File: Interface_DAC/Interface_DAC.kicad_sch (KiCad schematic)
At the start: 57 parts, among them SW1 SW_Push, SW2 SW_DIP_x02, U1 MIMXRT1011DAE5A, U2 W25Q32JVUU, U3 UM803RS, Y1 KC2520Z, Y2 KC2520Z, Y3 24M

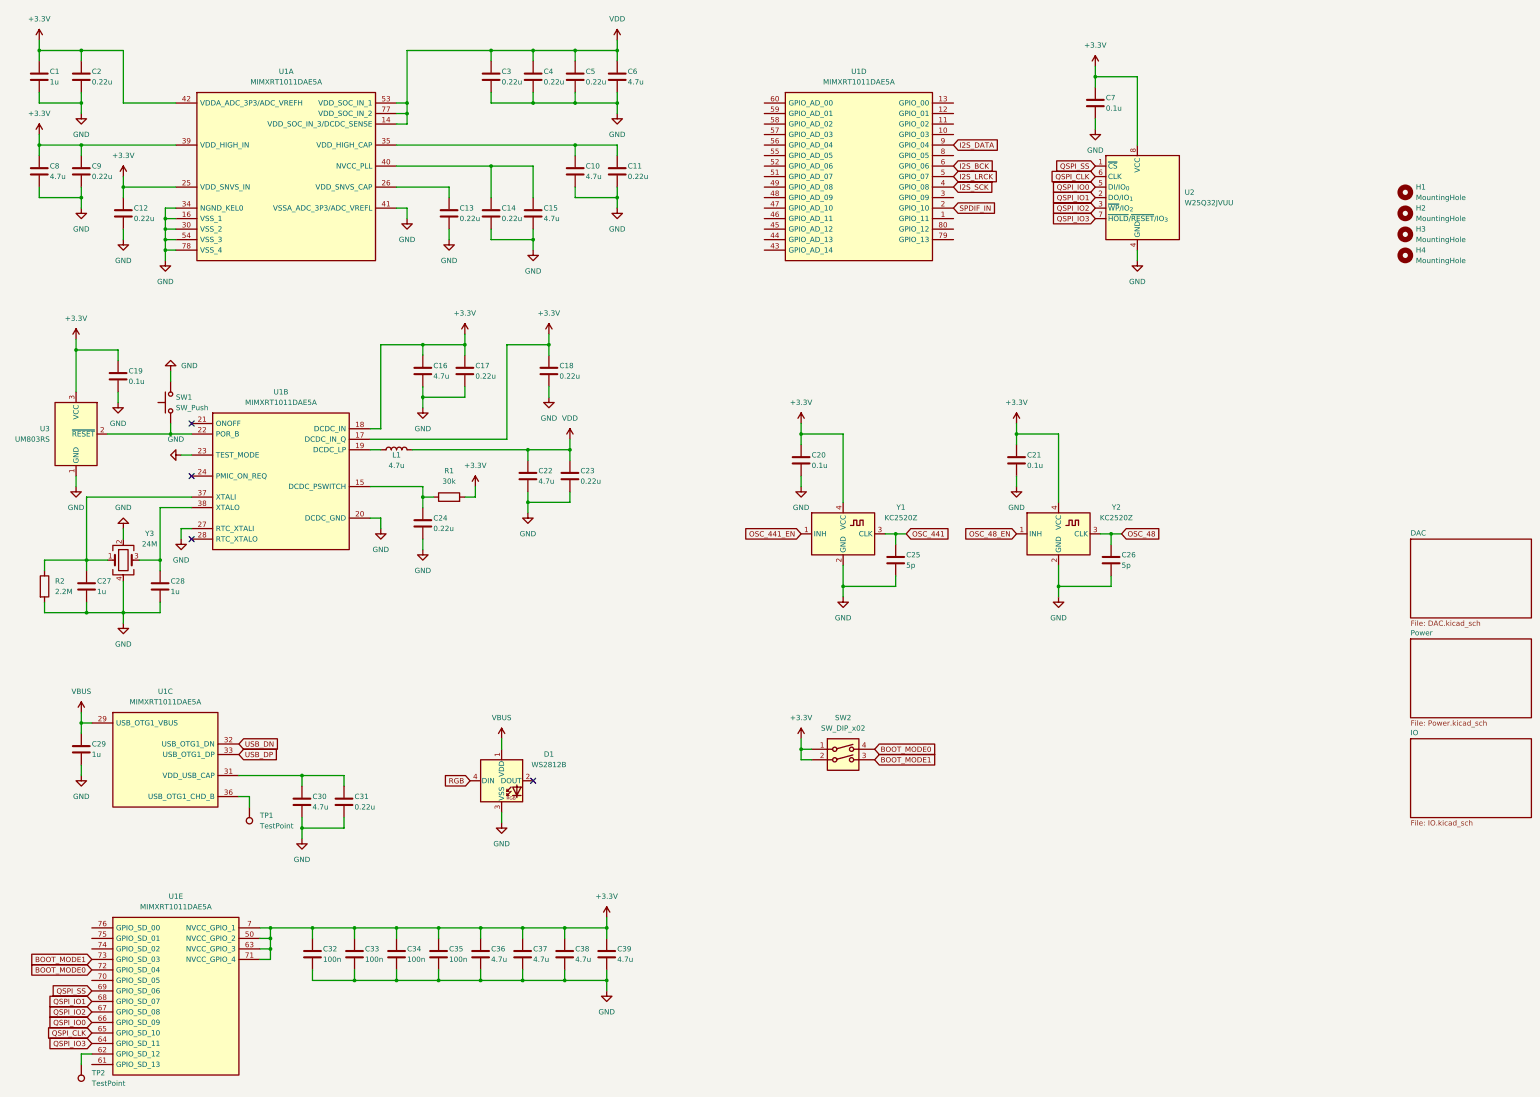
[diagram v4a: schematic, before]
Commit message: Microcontroller Swap
Changed the microcontroller from NXP MIMXRT1011DAE5A to ST STM32F446RET6
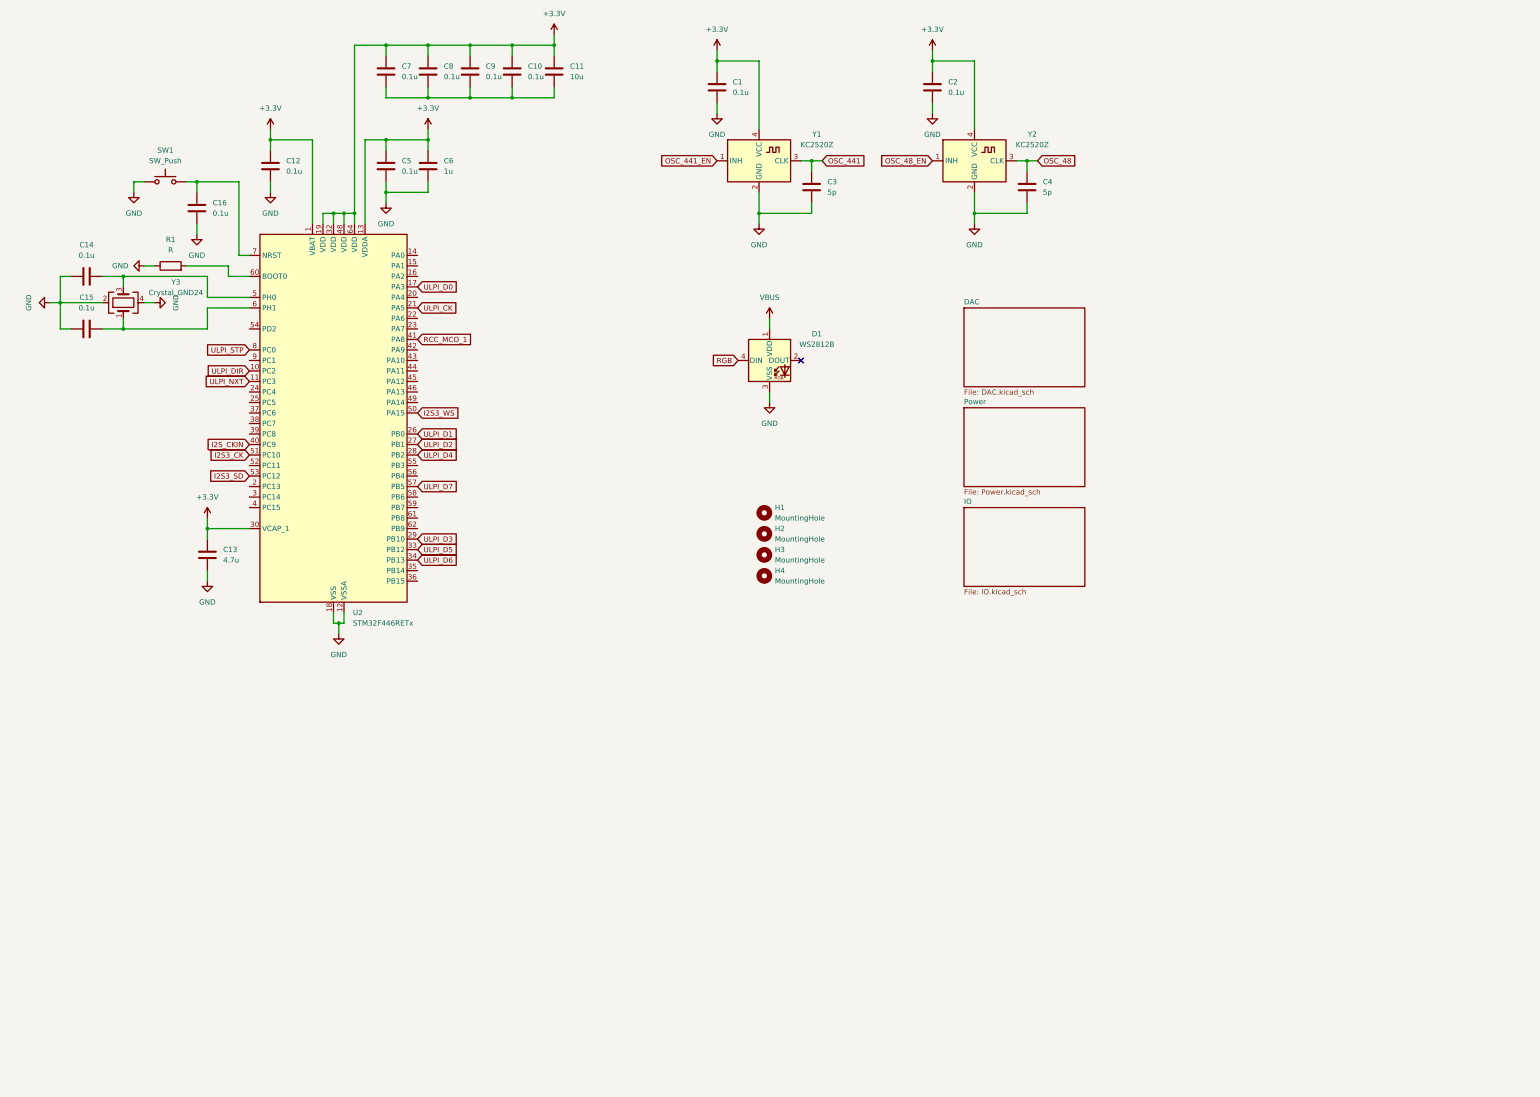
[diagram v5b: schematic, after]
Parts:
- removed C17, C18, C23, C24, C31: 0.22u, Capacitor_SMD:C_0402_1005Metric, symbol Device:C
- removed C19, C20, C21: 0.1u, Capacitor_SMD:C_0402_1005Metric, symbol Device:C
- removed C22, C30, C36, C37, C38, C39: 4.7u, Capacitor_SMD:C_0402_1005Metric, symbol Device:C
- removed C25, C26: 5p, Capacitor_SMD:C_0402_1005Metric, symbol Device:C
- removed C27, C28, C29: 1u, Capacitor_SMD:C_0402_1005Metric, symbol Device:C
- removed C32, C33, C34, C35: 100n, Capacitor_SMD:C_0402_1005Metric, symbol Device:C
- removed L1: 4.7u, Inductor_SMD:L_Murata_DFE201610P, symbol Device:L
- removed R2: 2.2M, Resistor_SMD:R_0402_1005Metric, symbol Device:R
- removed SW2: SW_DIP_x02, Button_Switch_SMD:SW_DIP_SPSTx02_Slide_Copal_CHS-02B_W7.62mm_P1.27mm, symbol Switch:SW_DIP_x02
- removed TP1, TP2: TestPoint, TestPoint:TestPoint_Pad_D1.0mm, symbol Connector:TestPoint
- removed U1: MIMXRT1011DAE5A, Package_QFP:LQFP-80_12x12mm_P0.5mm, symbol utils:MIMXRT1011DAE5A
- removed U2: W25Q32JVUU, Package_SON:Winbond_USON-8-2EP_3x4mm_P0.8mm_EP0.2x0.8mm, symbol Memory_Flash:W25Q32JVSS
- removed U3: UM803RS, Package_TO_SOT_SMD:SOT-23, symbol utils:UM803RS
- added U2: STM32F446RETx, Package_QFP:LQFP-64_10x10mm_P0.5mm, symbol MCU_ST_STM32F4:STM32F446RETx
- C1: value 1u -> 0.1u; footprint Capacitor_SMD:C_0402_1005Metric -> (none)
- C10, C15, C16, C8: value 4.7u -> 0.1u; footprint Capacitor_SMD:C_0402_1005Metric -> (none)
- C11: value 0.22u -> 10u; footprint Capacitor_SMD:C_0402_1005Metric -> (none)
- C12, C14, C2, C5, C9: value 0.22u -> 0.1u; footprint Capacitor_SMD:C_0402_1005Metric -> (none)
- C13: value 0.22u -> 4.7u; footprint Capacitor_SMD:C_0402_1005Metric -> (none)
- C3, C4: value 0.22u -> 5p; footprint Capacitor_SMD:C_0402_1005Metric -> (none)
- C6: value 4.7u -> 1u; footprint Capacitor_SMD:C_0402_1005Metric -> (none)
- C7: footprint Capacitor_SMD:C_0402_1005Metric -> (none)
- R1: value 30k -> R; footprint Resistor_SMD:R_0402_1005Metric -> (none)
- SW1: footprint Connector_PinHeader_1.27mm:PinHeader_1x02_P1.27mm_Vertical -> (none)
- Y3: value 24M -> Crystal_GND24; footprint Oscillator:Oscillator_SMD_Kyocera_KC2520Z-4Pin_2.5x2.0mm -> (none)
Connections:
- net +3.3V: now also C10.1, C11.1, C13.1, C5.1, C6.1, U2.1 (VBAT), U2.13 (VDDA), U2.19 (VDD), U2.30 (VCAP_1), U2.32 (VDD), U2.48 (VDD), U2.64 (VDD); no longer C16.1, R1.2
- net GND: now also C14.1, C15.1, R1.1, SW1.1, U2.12 (VSSA), U2.18 (VSS), U2.31 (VSS), U2.47 (VSS), U2.63 (VSS); no longer C10.2, C11.2, C14.2, C15.2, C7.2, C8.2, C9.2, SW1.2
- net OSC_441: now also C3.1
- net OSC_48: now also C4.1
- net at Y3.1: now also C15.2, U2.6 (PH1)
- net at Y3.3: now also C14.2, U2.5 (PH0)
- removed net VDD: C3.1, C4.1, C5.1, C6.1
- new net: C10.2, C11.2, C7.2, C8.2, C9.2
- new net: C16.1, SW1.2, U2.7 (NRST)
- new net: R1.2, U2.60 (BOOT0)
- new net I2S3_CK: U2.51 (PC10)
- new net I2S3_SD: U2.53 (PC12)
- new net I2S3_WS: U2.50 (PA15)
- new net I2S_CKIN: U2.40 (PC9)
- new net RCC_MCO_1: U2.41 (PA8)
- new net ULPI_CK: U2.21 (PA5)
- new net ULPI_D0: U2.17 (PA3)
- new net ULPI_D1: U2.26 (PB0)
- new net ULPI_D2: U2.27 (PB1)
- new net ULPI_D3: U2.29 (PB10)
- new net ULPI_D4: U2.28 (PB2)
- new net ULPI_D5: U2.33 (PB12)
- new net ULPI_D6: U2.34 (PB13)
- new net ULPI_D7: U2.57 (PB5)
- new net ULPI_DIR: U2.10 (PC2)
- new net ULPI_NXT: U2.11 (PC3)
- new net ULPI_STP: U2.8 (PC0)
- no-connect marks 4 -> 1
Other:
- moved on the sheet: D1, H1, H2, H3, H4, Y1, Y2

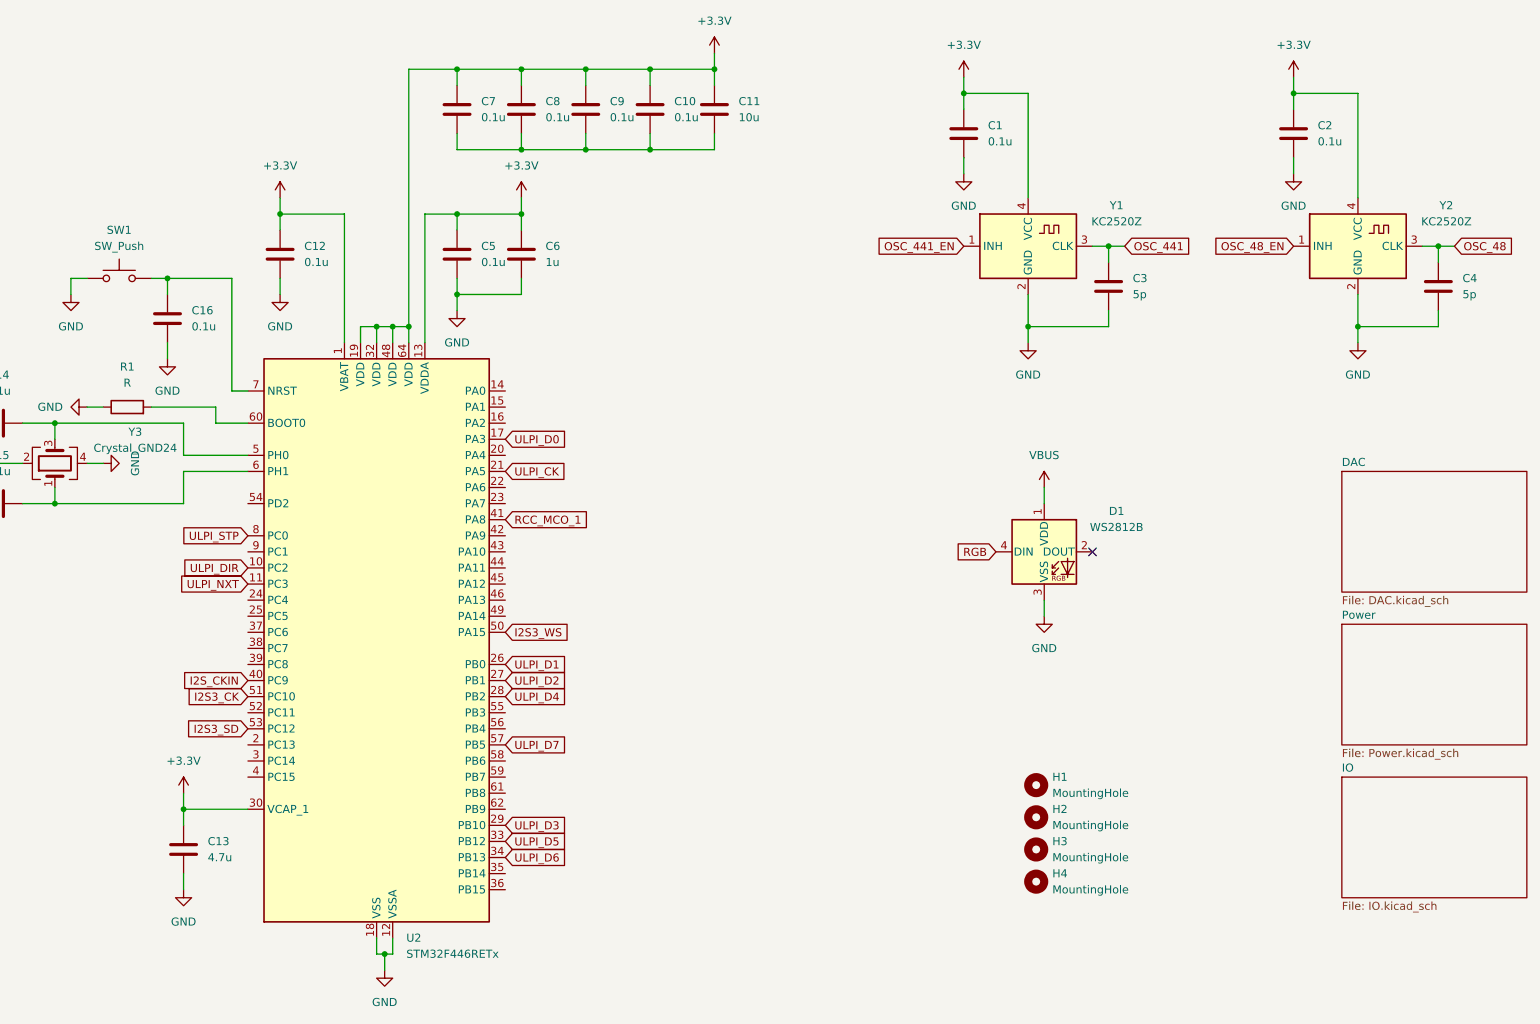
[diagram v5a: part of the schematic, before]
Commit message: Schematic Design and Library Relink
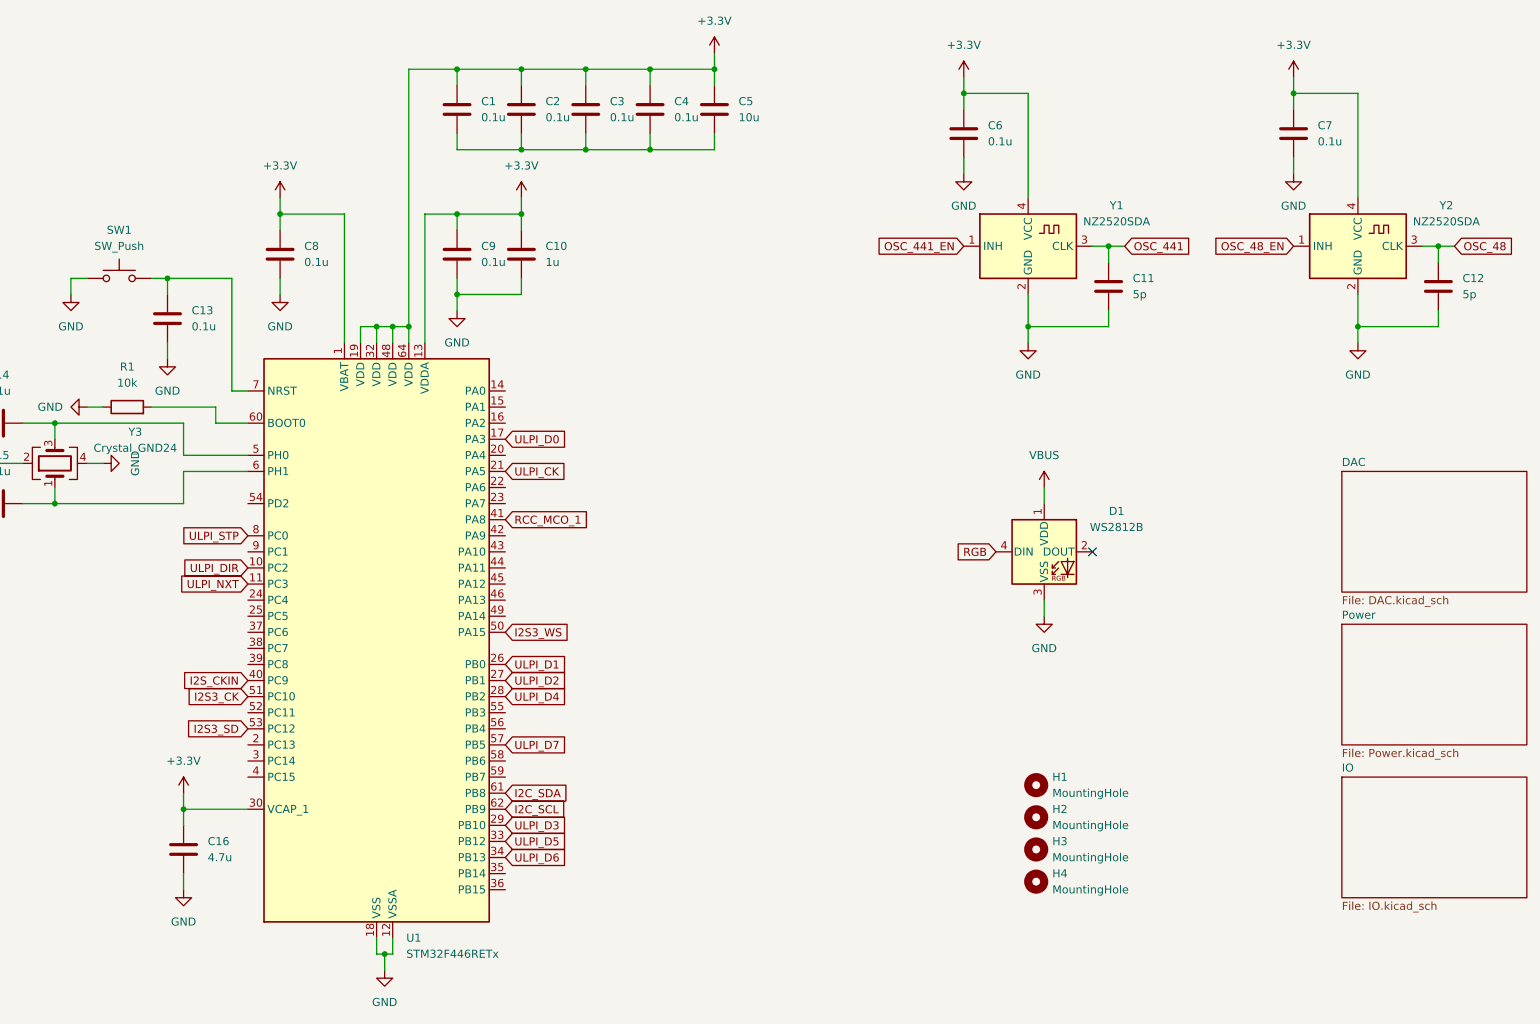
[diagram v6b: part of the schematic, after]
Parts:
- C1: renamed from C7; footprint (none) -> Capacitor_SMD:C_0402_1005Metric
- C10: renamed from C6; footprint (none) -> Capacitor_SMD:C_0402_1005Metric
- C11: renamed from C3; footprint (none) -> Capacitor_SMD:C_0402_1005Metric
- C12: renamed from C4; footprint (none) -> Capacitor_SMD:C_0402_1005Metric
- C13: renamed from C16; footprint (none) -> Capacitor_SMD:C_0402_1005Metric
- C14, C15: footprint (none) -> Capacitor_SMD:C_0402_1005Metric
- C16: renamed from C13; footprint (none) -> Capacitor_SMD:C_0402_1005Metric
- C2: renamed from C8; footprint (none) -> Capacitor_SMD:C_0402_1005Metric
- C3: renamed from C9; footprint (none) -> Capacitor_SMD:C_0402_1005Metric
- C4: renamed from C10; footprint (none) -> Capacitor_SMD:C_0402_1005Metric
- C5: renamed from C11; footprint (none) -> Capacitor_SMD:C_0402_1005Metric
- C6: renamed from C1; footprint (none) -> Capacitor_SMD:C_0402_1005Metric
- C7: renamed from C2; footprint (none) -> Capacitor_SMD:C_0402_1005Metric
- C8: renamed from C12; footprint (none) -> Capacitor_SMD:C_0402_1005Metric
- C9: renamed from C5; footprint (none) -> Capacitor_SMD:C_0402_1005Metric
- R1: value R -> 10k; footprint (none) -> Resistor_SMD:R_0402_1005Metric
- SW1: footprint (none) -> Connector_PinSocket_1.27mm:PinSocket_1x02_P1.27mm_Vertical
- Y1, Y2: value KC2520Z -> NZ2520SDA; footprint Oscillator:Oscillator_SMD_Kyocera_KC2520Z-4Pin_2.5x2.0mm -> Crystal:Crystal_SMD_2520-4Pin_2.5x2.0mm
- Y3: footprint (none) -> Crystal:Crystal_SMD_2016-4Pin_2.0x1.6mm
- renumbered U2 to U1
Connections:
- net I2C_SDA: now reaches U1.61 (PB8)
- net I2C_SCL: now reaches U1.62 (PB9)

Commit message: Schematic Design
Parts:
- added R2: 1M, Resistor_SMD:R_0402_1005Metric, symbol Device:R
- C14, C15: value 0.1u -> 8p
- Y3: value Crystal_GND24 -> 24M
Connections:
- net GND: now also C14.2, C15.2; no longer C14.1, C15.1
- net at U1.5 (PH0), Y3.3: now also C14.1, R2.2; no longer C14.2
- net at U1.6 (PH1), Y3.1: now also C15.1, R2.1; no longer C15.2
- net RCC_MCO_1: no longer names the net of U1.41 (PA8)
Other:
- moved on the sheet: R1
